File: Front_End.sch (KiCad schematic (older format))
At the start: 17 parts

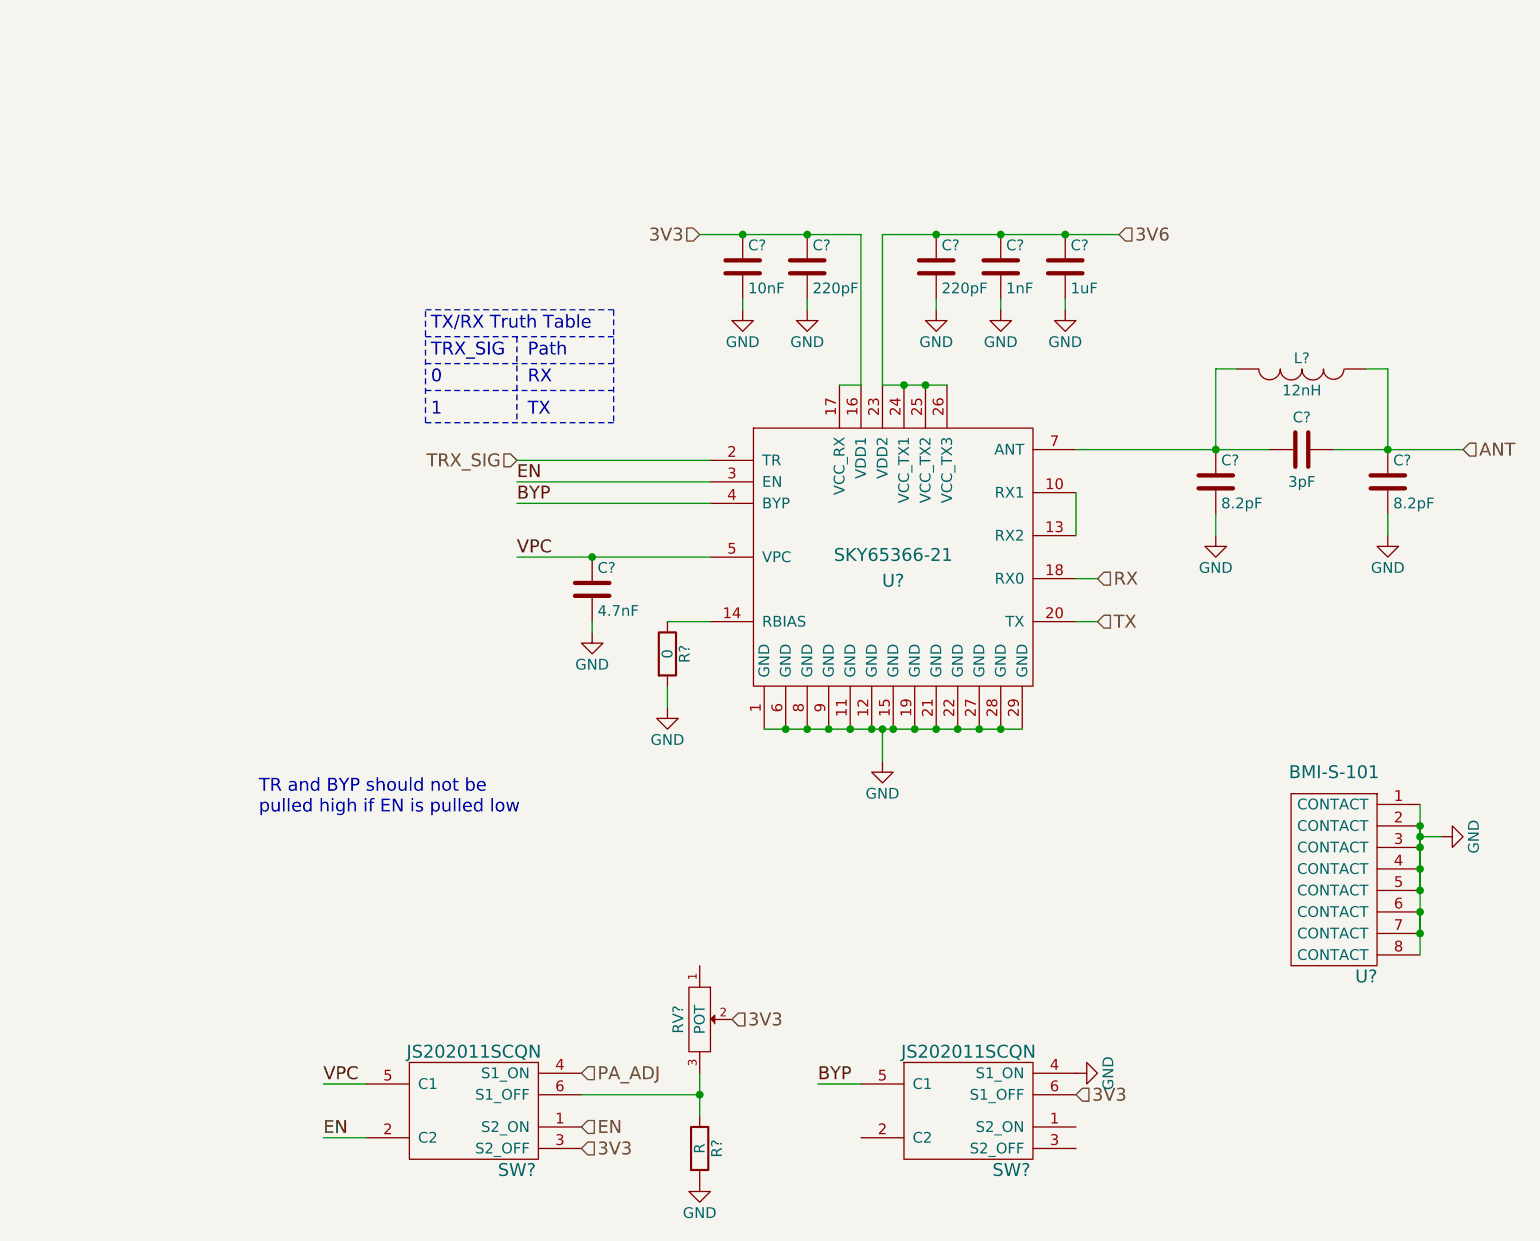
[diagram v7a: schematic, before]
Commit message: added a bunch of footprints and generated layout file
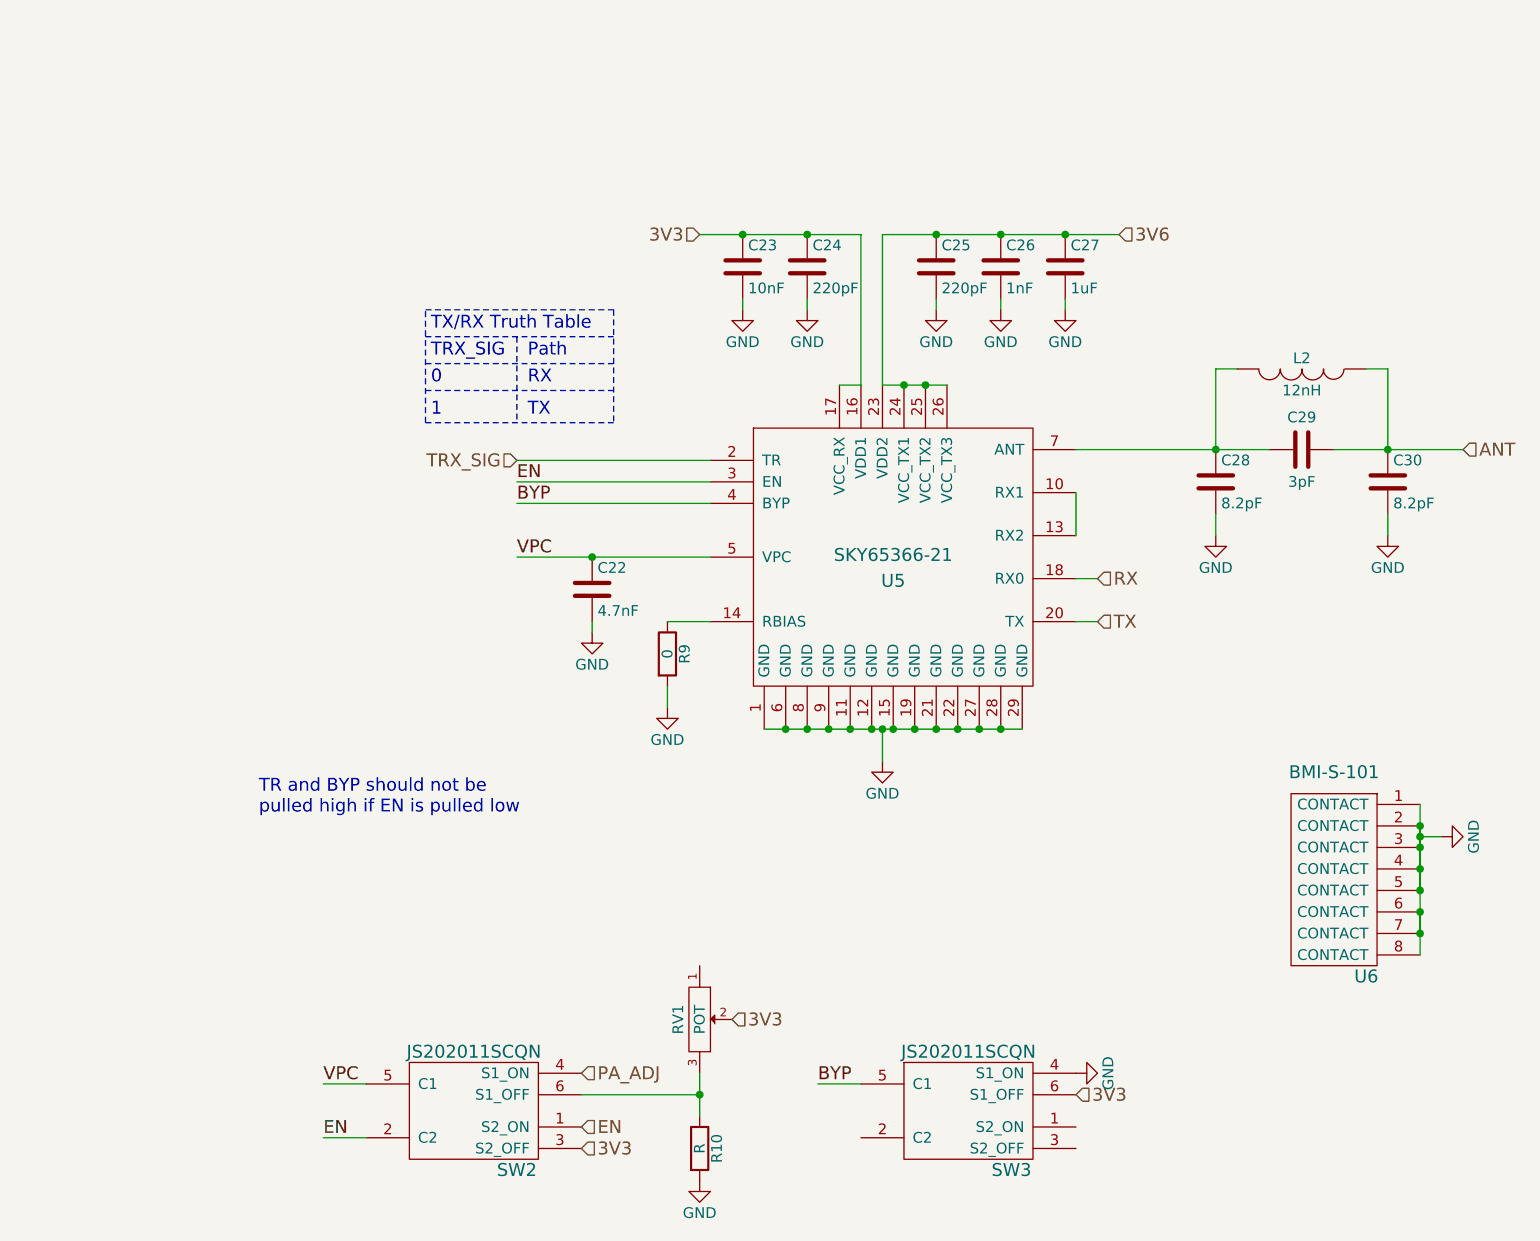
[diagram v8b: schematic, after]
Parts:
- C22, C23, C24, C25, C26, C27: renamed from C?; footprint (none) -> Capacitors_SMD:C_0402
- R10, R9: renamed from R?; footprint (none) -> Resistors_SMD:R_0402
- RV1: renamed from RV?; footprint (none) -> Resistors_SMD:R_0402
- SW2, SW3: renamed from SW?; footprint (none) -> SFUSat-Radio:JS2020_SMD
- U5: renamed from U?; footprint (none) -> SFUSat-Radio:MCM-28
- U6: renamed from U?; footprint (none) -> SFUSat-Radio:BMI-S-101
- gave numbers to parts that had none: 4
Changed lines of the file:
@@
 RX
 $Comp
-L SKY65366-21 U?
+L SKY65366-21 U5
 U 1 1 58719E85
 P 5550 3750
-F 0 "U?" H 5550 3725 60  0000 C TNN
+F 0 "U5" H 5550 3725 60  0000 C TNN
 F 1 "SKY65366-21" H 5550 3775 60  0000 C BNN
-F 2 "" H 5550 3650 60  0000 C CNN
+F 2 "SFUSat-Radio:MCM-28" H 5550 3650 60  0001 C CNN
 F 3 "" H 5550 3650 60  0000 C CNN
 	1    5550 3750
@@
 $EndComp
 $Comp
-L GND #PWR021
+L GND #PWR028
 U 1 1 58719F72
 P 5500 4650
-F 0 "#PWR021" H 5500 4400 50  0001 C CNN
+F 0 "#PWR028" H 5500 4400 50  0001 C CNN
 F 1 "GND" H 5500 4500 50  0000 C CNN
 F 2 "" H 5500 4650 50  0000 C CNN
@@
 3V6
 $Comp
-L C C?
+L C C25
 U 1 1 5871B9DF
 P 5750 2350
-F 0 "C?" H 5775 2450 50  0000 L CNN
+F 0 "C25" H 5775 2450 50  0000 L CNN
 F 1 "220pF" H 5775 2250 50  0000 L CNN
-F 2 "" H 5788 2200 50  0000 C CNN
+F 2 "Capacitors_SMD:C_0402" H 5788 2200 50  0001 C CNN
 F 3 "" H 5750 2350 50  0000 C CNN
 	1    5750 2350
@@
 $EndComp
 $Comp
-L C C?
+L C C26
 U 1 1 5871BA4C
 P 6050 2350
-F 0 "C?" H 6075 2450 50  0000 L CNN
+F 0 "C26" H 6075 2450 50  0000 L CNN
 F 1 "1nF" H 6075 2250 50  0000 L CNN
-F 2 "" H 6088 2200 50  0000 C CNN
+F 2 "Capacitors_SMD:C_0402" H 6088 2200 50  0001 C CNN
 F 3 "" H 6050 2350 50  0000 C CNN
 	1    6050 2350
@@
 $EndComp
 $Comp
-L C C?
+L C C27
 U 1 1 5871BAAB
 P 6350 2350
-F 0 "C?" H 6375 2450 50  0000 L CNN
+F 0 "C27" H 6375 2450 50  0000 L CNN
 F 1 "1uF" H 6375 2250 50  0000 L CNN
-F 2 "" H 6388 2200 50  0000 C CNN
+F 2 "Capacitors_SMD:C_0402" H 6388 2200 50  0001 C CNN
 F 3 "" H 6350 2350 50  0000 C CNN
 	1    6350 2350
@@
 $EndComp
 $Comp
-L GND #PWR022
+L GND #PWR029
 U 1 1 5871BAFA
 P 5750 2550
-F 0 "#PWR022" H 5750 2300 50  0001 C CNN
+F 0 "#PWR029" H 5750 2300 50  0001 C CNN
 F 1 "GND" H 5750 2400 50  0000 C CNN
 F 2 "" H 5750 2550 50  0000 C CNN
@@
 $EndComp
 $Comp
-L GND #PWR023
+L GND #PWR030
 U 1 1 5871BB16
 P 6050 2550
-F 0 "#PWR023" H 6050 2300 50  0001 C CNN
+F 0 "#PWR030" H 6050 2300 50  0001 C CNN
 F 1 "GND" H 6050 2400 50  0000 C CNN
 F 2 "" H 6050 2550 50  0000 C CNN
@@
 $EndComp
 $Comp
-L GND #PWR024
+L GND #PWR031
 U 1 1 5871BB32
 P 6350 2550
-F 0 "#PWR024" H 6350 2300 50  0001 C CNN
+F 0 "#PWR031" H 6350 2300 50  0001 C CNN
 F 1 "GND" H 6350 2400 50  0000 C CNN
 F 2 "" H 6350 2550 50  0000 C CNN
@@
 Connection ~ 5700 2900
 $Comp
-L C C?
+L C C24
 U 1 1 5871BCCF
 P 5150 2350
-F 0 "C?" H 5175 2450 50  0000 L CNN
+F 0 "C24" H 5175 2450 50  0000 L CNN
 F 1 "220pF" H 5175 2250 50  0000 L CNN
-F 2 "" H 5188 2200 50  0000 C CNN
+F 2 "Capacitors_SMD:C_0402" H 5188 2200 50  0001 C CNN
 F 3 "" H 5150 2350 50  0000 C CNN
 	1    5150 2350
@@
 $EndComp
 $Comp
-L C C?
+L C C23
 U 1 1 5871BD40
 P 4850 2350
-F 0 "C?" H 4875 2450 50  0000 L CNN
+F 0 "C23" H 4875 2450 50  0000 L CNN
 F 1 "10nF" H 4875 2250 50  0000 L CNN
-F 2 "" H 4888 2200 50  0000 C CNN
+F 2 "Capacitors_SMD:C_0402" H 4888 2200 50  0001 C CNN
 F 3 "" H 4850 2350 50  0000 C CNN
 	1    4850 2350
@@
 $EndComp
 $Comp
-L GND #PWR025
+L GND #PWR032
 U 1 1 5871BD81
 P 5150 2550
-F 0 "#PWR025" H 5150 2300 50  0001 C CNN
+F 0 "#PWR032" H 5150 2300 50  0001 C CNN
 F 1 "GND" H 5150 2400 50  0000 C CNN
 F 2 "" H 5150 2550 50  0000 C CNN
@@
 $EndComp
 $Comp
-L GND #PWR026
+L GND #PWR033
 U 1 1 5871BDA1
 P 4850 2550
-F 0 "#PWR026" H 4850 2300 50  0001 C CNN
+F 0 "#PWR033" H 4850 2300 50  0001 C CNN
 F 1 "GND" H 4850 2400 50  0000 C CNN
 F 2 "" H 4850 2550 50  0000 C CNN
@@
 	6400 3400 6400 3600
 $Comp
-L C C?
+L C C29
 U 1 1 5871C0B1
 P 7450 3200
-F 0 "C?" V 7300 3200 50  0000 C CNN
+F 0 "C29" V 7300 3200 50  0000 C CNN
 F 1 "3pF" V 7600 3200 50  0000 C CNN
-F 2 "" H 7488 3050 50  0000 C CNN
+F 2 "" H 7488 3050 50  0001 C CNN
 F 3 "" H 7450 3200 50  0000 C CNN
 	1    7450 3200
@@
 $EndComp
 $Comp
-L C C?
+L C C28
 U 1 1 5871C0F0
 P 7050 3350
-F 0 "C?" H 7075 3450 50  0000 L CNN
+F 0 "C28" H 7075 3450 50  0000 L CNN
 F 1 "8.2pF" H 7075 3250 50  0000 L CNN
-F 2 "" H 7088 3200 50  0000 C CNN
+F 2 "" H 7088 3200 50  0001 C CNN
 F 3 "" H 7050 3350 50  0000 C CNN
 	1    7050 3350
@@
 $EndComp
 $Comp
-L C C?
+L C C30
 U 1 1 5871C127
 P 7850 3350
-F 0 "C?" H 7875 3450 50  0000 L CNN
+F 0 "C30" H 7875 3450 50  0000 L CNN
 F 1 "8.2pF" H 7875 3250 50  0000 L CNN
-F 2 "" H 7888 3200 50  0000 C CNN
+F 2 "" H 7888 3200 50  0001 C CNN
 F 3 "" H 7850 3350 50  0000 C CNN
 	1    7850 3350
@@
 $EndComp
 $Comp
-L INDUCTOR L?
+L INDUCTOR L2
 U 1 1 5871C1AA
 P 7450 2825
-F 0 "L?" V 7400 2825 50  0000 C CNN
+F 0 "L2" V 7400 2825 50  0000 C CNN
 F 1 "12nH" V 7550 2825 50  0000 C CNN
-F 2 "" H 7450 2825 50  0000 C CNN
+F 2 "" H 7450 2825 50  0001 C CNN
 F 3 "" H 7450 2825 50  0000 C CNN
 	1    7450 2825
@@
 	7050 2825 7050 3200
 $Comp
-L GND #PWR027
+L GND #PWR034
 U 1 1 5871C376
 P 7050 3600
-F 0 "#PWR027" H 7050 3350 50  0001 C CNN
+F 0 "#PWR034" H 7050 3350 50  0001 C CNN
 F 1 "GND" H 7050 3450 50  0000 C CNN
 F 2 "" H 7050 3600 50  0000 C CNN
@@
 $EndComp
 $Comp
-L GND #PWR028
+L GND #PWR035
 U 1 1 5871C39E
 P 7850 3600
-F 0 "#PWR028" H 7850 3350 50  0001 C CNN
+F 0 "#PWR035" H 7850 3350 50  0001 C CNN
 F 1 "GND" H 7850 3450 50  0000 C CNN
 F 2 "" H 7850 3600 50  0000 C CNN
@@
 	7050 3500 7050 3600
 $Comp
-L R R?
+L R R9
 U 1 1 5871C966
 P 4500 4150
-F 0 "R?" V 4580 4150 50  0000 C CNN
+F 0 "R9" V 4580 4150 50  0000 C CNN
 F 1 "0" V 4500 4150 50  0000 C CNN
-F 2 "" V 4430 4150 50  0000 C CNN
+F 2 "Resistors_SMD:R_0402" V 4430 4150 50  0001 C CNN
 F 3 "" H 4500 4150 50  0000 C CNN
 	1    4500 4150
@@
 $EndComp
 $Comp
-L GND #PWR029
+L GND #PWR036
 U 1 1 5871CA19
 P 4500 4400
-F 0 "#PWR029" H 4500 4150 50  0001 C CNN
+F 0 "#PWR036" H 4500 4150 50  0001 C CNN
 F 1 "GND" H 4500 4250 50  0000 C CNN
 F 2 "" H 4500 4400 50  0000 C CNN
@@
 	4500 4300 4500 4400
 $Comp
-L C C?
+L C C22
 U 1 1 5871CCE4
 P 4150 3850
-F 0 "C?" H 4175 3950 50  0000 L CNN
+F 0 "C22" H 4175 3950 50  0000 L CNN
 F 1 "4.7nF" H 4175 3750 50  0000 L CNN
-F 2 "" H 4188 3700 50  0000 C CNN
+F 2 "Capacitors_SMD:C_0402" H 4188 3700 50  0001 C CNN
 F 3 "" H 4150 3850 50  0000 C CNN
 	1    4150 3850
@@
 $EndComp
 $Comp
-L GND #PWR030
+L GND #PWR037
 U 1 1 5871CD23
 P 4150 4050
-F 0 "#PWR030" H 4150 3800 50  0001 C CNN
+F 0 "#PWR037" H 4150 3800 50  0001 C CNN
 F 1 "GND" H 4150 3900 50  0000 C CNN
 F 2 "" H 4150 4050 50  0000 C CNN
@@
 	7750 2825 7850 2825
 $Comp
-L R R?
+L R R10
 U 1 1 587C3C10
 P 4650 6450
-F 0 "R?" V 4730 6450 50  0000 C CNN
+F 0 "R10" V 4730 6450 50  0000 C CNN
 F 1 "R" V 4650 6450 50  0000 C CNN
-F 2 "" V 4580 6450 50  0000 C CNN
+F 2 "Resistors_SMD:R_0402" V 4580 6450 50  0001 C CNN
 F 3 "" H 4650 6450 50  0000 C CNN
 	1    4650 6450
@@
 $EndComp
 $Comp
-L GND #PWR?
+L GND #PWR038
 U 1 1 587C3C45
 P 4650 6600
-F 0 "#PWR?" H 4650 6350 50  0001 C CNN
+F 0 "#PWR038" H 4650 6350 50  0001 C CNN
 F 1 "GND" H 4650 6450 50  0000 C CNN
 F 2 "" H 4650 6600 50  0000 C CNN
@@
 3V3
 $Comp
-L POT RV?
+L POT RV1
 U 1 1 587CA745
 P 4650 5850
-F 0 "RV?" H 4650 5750 50  0000 C CNN
+F 0 "RV1" H 4650 5750 50  0000 C CNN
 F 1 "POT" H 4650 5850 50  0000 C CNN
-F 2 "" H 4650 5850 50  0000 C CNN
+F 2 "Resistors_SMD:R_0402" H 4650 5850 50  0001 C CNN
 F 3 "" H 4650 5850 50  0000 C CNN
 	1    4650 5850
@@
 $EndComp
 $Comp
-L JS202011SCQN SW?
+L JS202011SCQN SW2
 U 1 1 587E3043
 P 3600 6150
-F 0 "SW?" H 3800 5750 60  0000 C CNN
+F 0 "SW2" H 3800 5750 60  0000 C CNN
 F 1 "JS202011SCQN" H 3600 6300 60  0000 C CNN
-F 2 "" H 3600 6150 60  0000 C CNN
+F 2 "SFUSat-Radio:JS2020_SMD" H 3600 6150 60  0001 C CNN
 F 3 "" H 3600 6150 60  0000 C CNN
 	1    3600 6150
@@
 TR and BYP should not be \npulled high if EN is pulled low
 $Comp
-L JS202011SCQN SW?
+L JS202011SCQN SW3
 U 1 1 58828A5A
 P 5900 6150
-F 0 "SW?" H 6100 5750 60  0000 C CNN
+F 0 "SW3" H 6100 5750 60  0000 C CNN
 F 1 "JS202011SCQN" H 5900 6300 60  0000 C CNN
-F 2 "" H 5900 6150 60  0000 C CNN
+F 2 "SFUSat-Radio:JS2020_SMD" H 5900 6150 60  0001 C CNN
 F 3 "" H 5900 6150 60  0000 C CNN
 	1    5900 6150
@@
 3V3
 $Comp
-L GND #PWR?
+L GND #PWR039
 U 1 1 58829BDE
 P 6400 6100
-F 0 "#PWR?" H 6400 5850 50  0001 C CNN
+F 0 "#PWR039" H 6400 5850 50  0001 C CNN
 F 1 "GND" H 6400 5950 50  0000 C CNN
 F 2 "" H 6400 6100 50  0000 C CNN
@@
 $EndComp
 $Comp
-L BMI-S-101 U?
+L BMI-S-101 U6
 U 1 1 5882B6C7
 P 7600 4850
-F 0 "U?" H 7750 4050 60  0000 C CNN
+F 0 "U6" H 7750 4050 60  0000 C CNN
 F 1 "BMI-S-101" H 7600 5000 60  0000 C CNN
-F 2 "" H 7600 4850 60  0000 C CNN
+F 2 "SFUSat-Radio:BMI-S-101" H 7600 4850 60  0001 C CNN
 F 3 "" H 7600 4850 60  0000 C CNN
 	1    7600 4850
@@
 $EndComp
 $Comp
-L GND #PWR?
+L GND #PWR040
 U 1 1 5882B8A8
 P 8100 5000
-F 0 "#PWR?" H 8100 4750 50  0001 C CNN
+F 0 "#PWR040" H 8100 4750 50  0001 C CNN
 F 1 "GND" H 8100 4850 50  0000 C CNN
 F 2 "" H 8100 5000 50  0000 C CNN
